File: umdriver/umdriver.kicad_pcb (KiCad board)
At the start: 2 copper layers, 100 x 90 mm, 81 parts, among them J1 SWD, J2 USB micro, J3 Isolated uart, Q1 Q_NMOS_GDS, SW1 SW_Reset, SW2 SW_Test, U1 STGIPQ8C60T, U2 NCP718, U3 ATSAMD21G18A-AUT, U4 SN65HVD72, U5 ISO7721, Y1 32.768

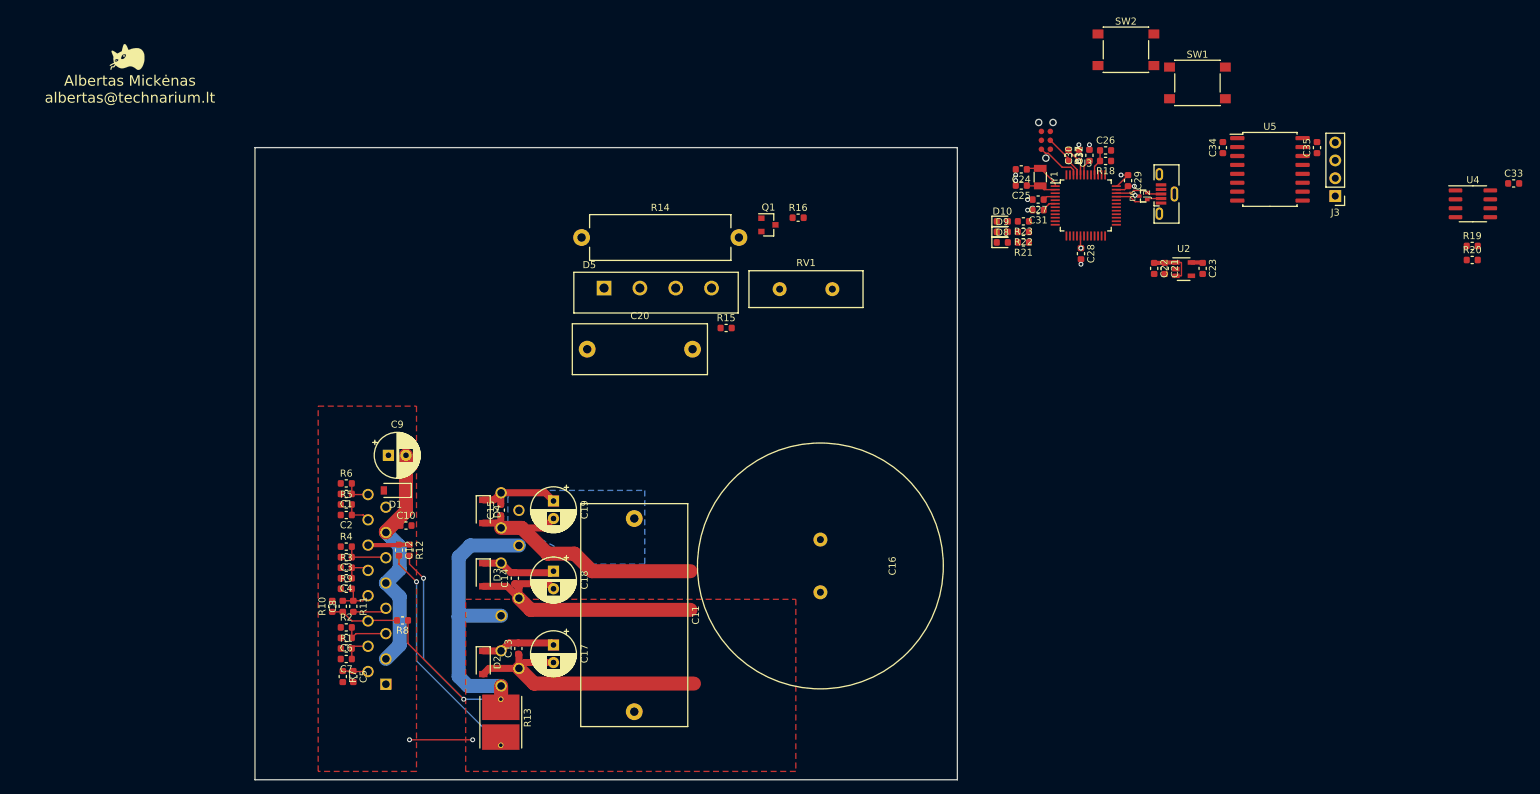
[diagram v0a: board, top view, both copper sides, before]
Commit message: Add battery monitoring, connect mcu lines to outside
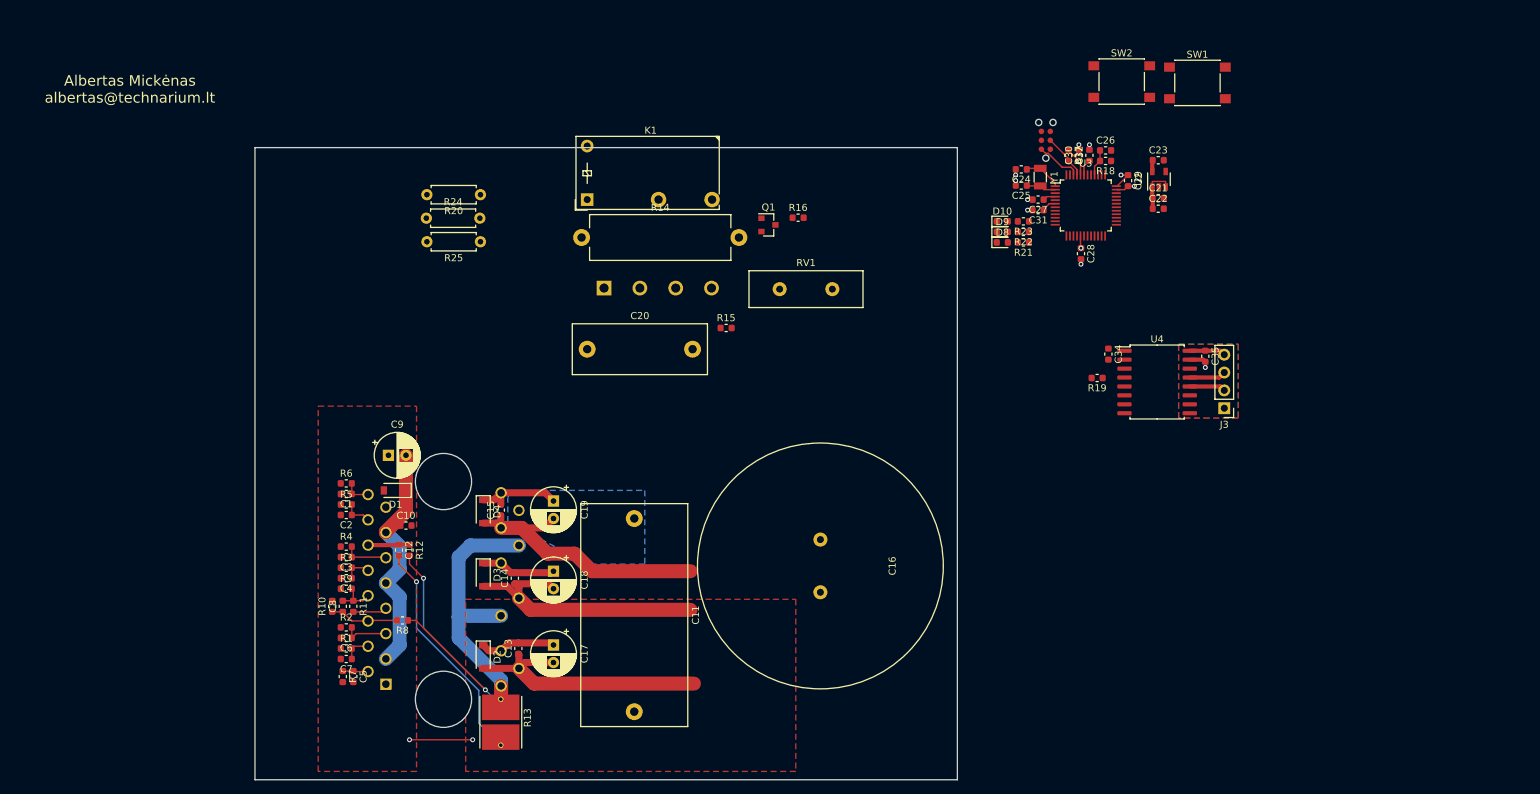
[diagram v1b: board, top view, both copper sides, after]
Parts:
- removed C33: 1u, Capacitor_SMD:C_0603_1608Metric
- removed D6: D_TVS_x2_AAC, miceuz-lib:SC89
- removed G***: LOGO, miceuz-lib:catnip
- removed J2: USB micro, Connectors_USB:USB_Micro-B_Vertical_Molex-105133-0001
- removed U5: ISO7721, Package_SO:SOIC-16W_7.5x10.3mm_P1.27mm
- added K1: FINDER-32.21-x000, Relay_THT:Relay_SPST_Finder_32.21-x300, F.Cu at (97.3, 47.4)
- added R24: R, Resistors_THT:R_Axial_DIN0207_L6.3mm_D2.5mm_P7.62mm_Horizontal, F.Cu at (74.4, 50.0)
- added R25: R, Resistors_THT:R_Axial_DIN0207_L6.3mm_D2.5mm_P7.62mm_Horizontal, F.Cu at (82.1, 53.4)
- D5: moved to B.Cu
- J3: value Isolated uart -> Isolated rs485
- R20: value 1M -> R; footprint Resistor_SMD:R_0603_1608Metric -> Resistors_THT:R_Axial_DIN0207_L6.3mm_D2.5mm_P7.62mm_Horizontal
- U4: value SN65HVD72 -> ISO3088DW; footprint Package_SO:SOIC-8_3.9x4.9mm_P1.27mm -> Package_SO:SOIC-16W_7.5x10.3mm_P1.27mm
- moved R20 141.5 mm to (82.1, 46.7), turned to 180 degrees
- moved R19 56.6 mm to (169.9, 72.8), turned to 180 degrees
- moved U4 51.6 mm to (178.4, 73.4)
- moved J3 34.1 mm to (188.0, 77.1)
- moved C35 33.7 mm to (185.3, 69.7), turned to -90 degrees
- moved C34 33.6 mm to (171.5, 69.4), turned to -90 degrees
- moved C23 16.6 mm to (178.6, 41.8), turned to 0 degrees
- moved U2 13.3 mm to (178.7, 44.5), turned to 90 degrees
- moved C21 10.0 mm to (178.6, 47.2), turned to 0 degrees
- moved C22 8.52 mm to (178.6, 48.7), turned to 0 degrees
- moved SW2 4.57 mm to (173.4, 30.6)
- moved D2 0.81 mm to (82.5, 112.5)
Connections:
- net /Microcontroller/RS485_DE renamed Net-(U3-Pad16)
- C35 pad 2: GND -> /Microcontroller/ISO_GND
- D5 pad 1: /Power Input/DCBUS -> VBUS
- D5 pad 4: /Power Input/GND -> GND
- J3 pad 2: /Microcontroller/ISO_TX -> /Microcontroller/ISO_A
- J3 pad 3: /Microcontroller/ISO_RX -> /Microcontroller/ISO_B
- Q1 pad 3: /Power Input/GND -> GND
- R16 pad 2: /Power Input/GND -> GND
- R19 pad 1: +3V3 -> /Microcontroller/~RS485_RE
- R19 pad 2: /Microcontroller/~RE -> GND
- R20 pad 1: /Microcontroller/DE -> VBUS
- R20 pad 2: GND -> Net-(R20-Pad2)
- U4 pad 1: /Microcontroller/RO -> +3V3
- U4 pad 2: /Microcontroller/~RE -> GND
- U4 pad 3: /Microcontroller/DE -> /Microcontroller/RX
- U4 pad 4: /Microcontroller/DI -> /Microcontroller/~RS485_RE
- U4 pad 5: GND -> /Microcontroller/~RS485_RE
- U4 pad 6: /Microcontroller/RS485A -> /Microcontroller/TX
- U4 pad 7: /Microcontroller/RS485B -> GND
- U4 pad 8: +3V3 -> GND
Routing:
- net /Microcontroller/D-: track 6.85 -> 0.00 mm
- net /Microcontroller/D+: track 6.74 -> 0.00 mm
- net /Microcontroller/ISO_B: track 0.00 -> 5.21 mm
- net /Microcontroller/ISO_VCC: track 0.00 -> 5.14 mm
- net /Microcontroller/ISO_A: track 0.00 -> 5.14 mm
- net /VSHUNT: track 85.5 -> 80.7 mm
- net /Microcontroller/ISO_GND: track 0.00 -> 2.33 mm, vias 0 -> 1
- net GND: vias 12 -> 11
- added copper zone on B.Cu, net /Microcontroller/ISO_GND
- added copper zone on F.Cu, net /Microcontroller/ISO_GND
